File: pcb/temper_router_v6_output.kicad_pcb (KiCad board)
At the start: 4 copper layers, 100 x 150 mm, 33 parts, among them Q1 IKW40N120H3, Q2 IKW40N120H3

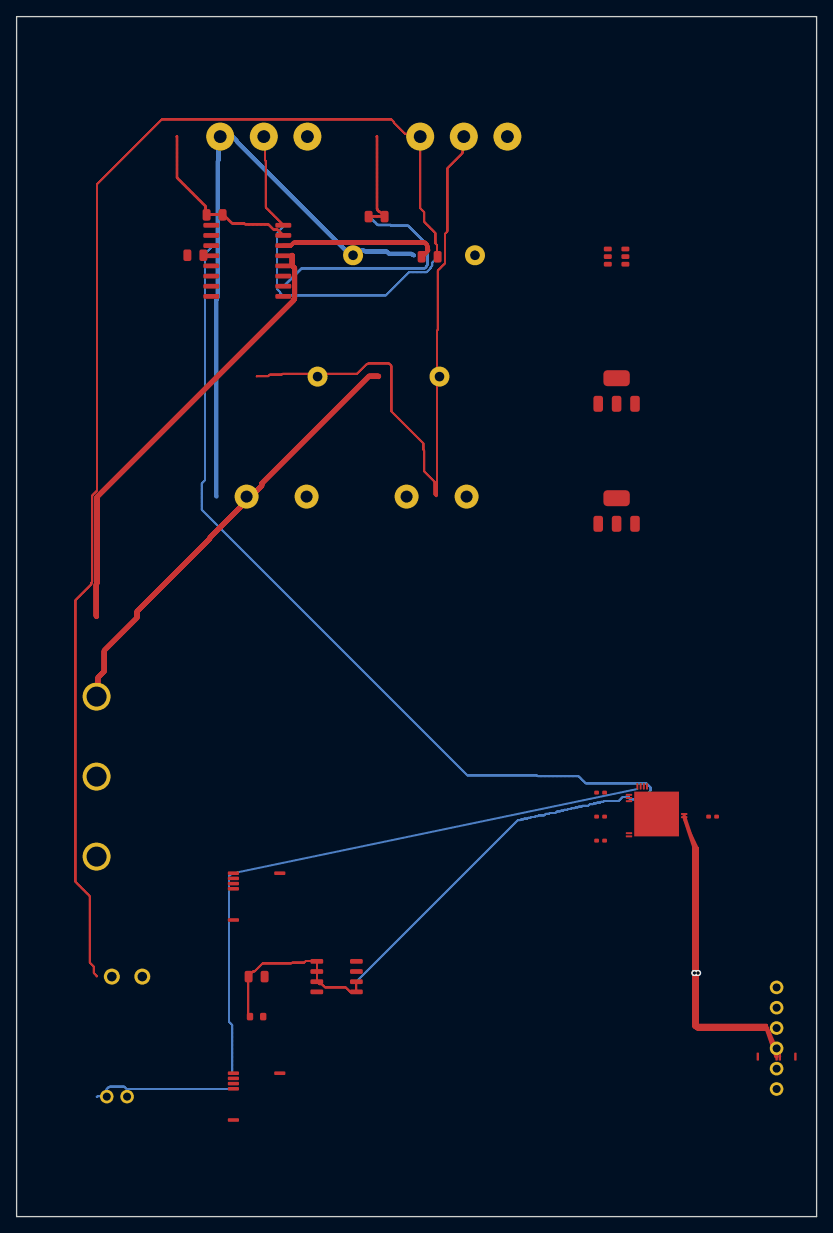
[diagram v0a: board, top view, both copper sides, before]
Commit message: fix: enable power plane export in Router V6
- Uncommented power plane (zone) export code in run_router_v6.py
- Router now exports GND plane for B.Cu layer
- DRC shows 1480 violations (similar to 1463 without zones)
- Power plane adds minimal new violations
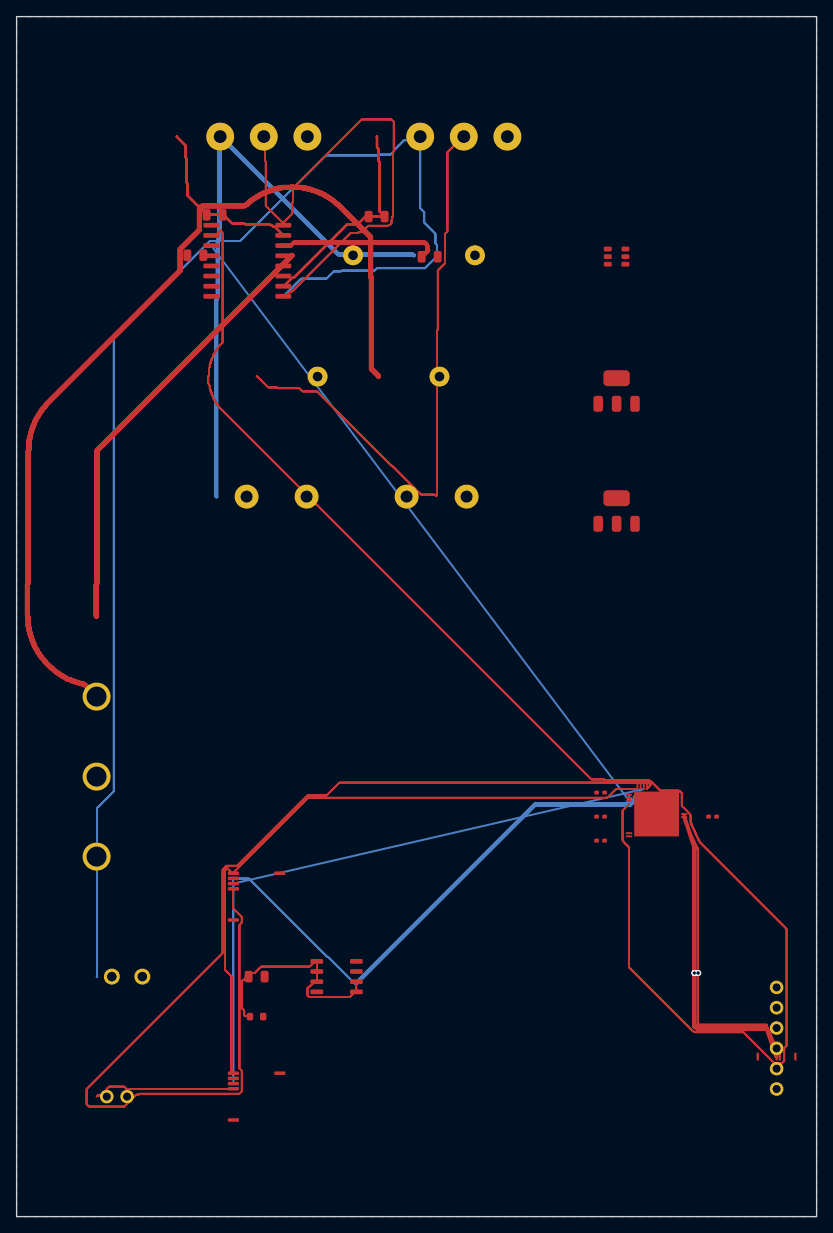
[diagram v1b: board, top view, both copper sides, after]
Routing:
- net PWM_H: track 0.00 -> 187.4 mm
- net SPI_CS_TEMP: track 0.00 -> 141.7 mm
- net SPI_MOSI: track 0.00 -> 92.1 mm
- net SPI_MISO: track 0.00 -> 77.6 mm
- net AC_N: track 55.4 -> 117.8 mm
- net SW_NODE: track 205.4 -> 230.4 mm
- net PWM_L: track 107.7 -> 86.8 mm
- net GATE_L: track 43.0 -> 26.7 mm
- net DC_BUS-: track 82.8 -> 75.2 mm
- net I_SENSE: track 67.7 -> 72.9 mm
- net SPI_CLK: track 77.2 -> 82.0 mm
- added copper zone on B.Cu, net GND
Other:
- copper layers 4 -> 2

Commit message: Major Cleanup: JAX Removal, Legacy Purge, and Structural Flattening
What:
- Removed JAX dependencies from the core placement and routing pipeline.
- Purged over 100 legacy files including 'ml/', 'topological/', 'router_v7/', and unused 'routing/' packages.
- Flattened the monorepo structure by removing the redundant 'src/' directory across all packages.
- Ported 'wirelength.py' to NumPy and standardized 'losses/' infrastructure.

Why:
- The project has moved from JAX-based differentiable optimization to a discrete Benders-V6 geometric approach.
- The 5-level deep directory nesting was identified as an anti-pattern and hindered maintainability.
- Consolidated the codebase to focus on the active, stable production pipeline.

How:
- Refactored 'spectral.py', 'state.py', 'base.py', and 'losses/wirelength.py' to use NumPy/SciPy.
- Batch removed obsolete optimization and experimental scripts.
- Physically moved package source code out of 'src/' and updated all 'pyproject.toml' (hatch/pytest/ruff) configurations.
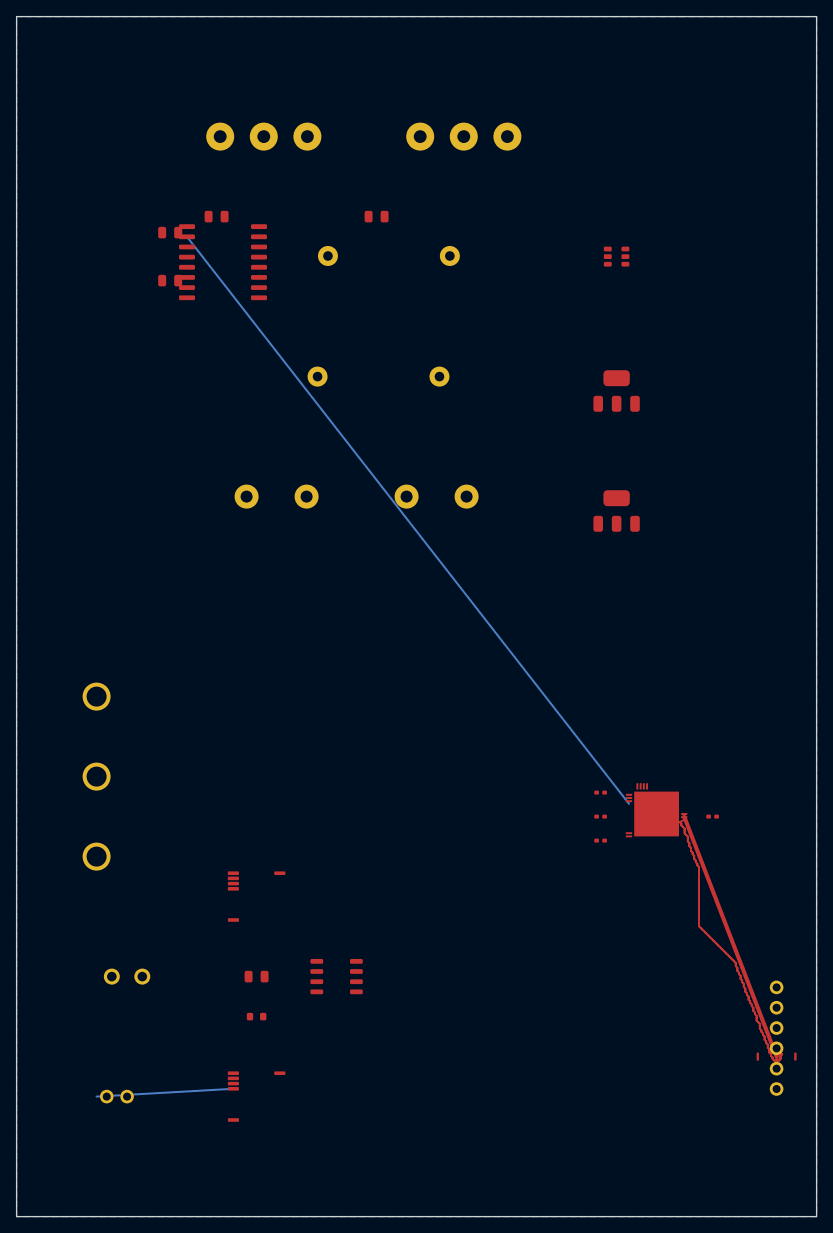
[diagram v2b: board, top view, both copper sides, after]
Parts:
- moved C_BOOT 32.6 mm to (19.2, 33.0)
- moved C_VCC 4.23 mm to (19.2, 27.0)
- moved D1 3.14 mm to (38.9, 29.9)
- moved U_GATE 3.04 mm to (25.8, 30.7)
- moved R_GATE_H 0.33 mm to (25.0, 25.0)
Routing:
- net SW_NODE: track 230.4 -> 0.00 mm
- net SPI_CS_TEMP: track 141.7 -> 0.00 mm
- net PWM_H: track 187.4 -> 89.9 mm
- net SPI_MOSI: track 92.1 -> 0.00 mm
- net PWM_L: track 86.8 -> 0.00 mm
- net SPI_CLK: track 82.0 -> 0.00 mm
- net SPI_MISO: track 77.6 -> 0.00 mm
- net DC_BUS+: track 75.7 -> 0.00 mm
- net DC_BUS-: track 75.2 -> 0.00 mm
- net I_SENSE: track 72.9 -> 0.00 mm
- net AC_N: track 117.8 -> 53.3 mm
- net GATE_L: track 26.7 -> 0.00 mm
- net GATE_H: track 22.1 -> 0.00 mm
- net VCC_BOOT: track 20.2 -> 0.00 mm
- net USB_D+: track 39.3 -> 32.1 mm, vias 1 -> 0
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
